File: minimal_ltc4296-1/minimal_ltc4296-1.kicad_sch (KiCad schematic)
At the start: 28 parts, among them Q1 100.0 V, Q2 100.0 V, Q3 100.0 V, U1 LTC4296AUK-1-PBF

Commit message: Update KiCad PCB and schematic files
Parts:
- added Q4, Q5: 100.0 V, transistor_footprints:LFPAK33-8, symbol TRANSISTORS_PSMN075-100MSEX_DATA_BASE:Q_PSMN075-100MSEX
- added Q6: 100.0 V, transistor_footprints:LFPAK33-8, symbol TRANSISTORS_PSMN040-100MSEX_DATA_BASE:Q_PSMN040-100MSEX
- added R17, R18: 24 mΩ, resistor_footprints:R_0612_1632Metric, symbol RESISTORS_ERJ-B2CF_DATA_BASE:R_ERJ-B2CFR024V
- added R19: 390 mΩ, resistor_footprints:R_0612_1632Metric, symbol RESISTORS_ERJ-B2BF_DATA_BASE:R_ERJ-B2BFR39V
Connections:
- net GND: no longer Q1.4 (G), U1.23 (LGATE)
- net PSE: now also U1.4 (HSNSP0), U1.44 (HSNSP2), U1.48 (HSNSP1), R17.1, R18.1, R19.1
- net OUTP0: now reaches U1.1 (OUTP0)
- net OUTP0: now also Q5.1 (S), Q5.2 (S), Q5.3 (S)
- net HGATE0: now reaches U1.2 (HGATE0)
- net HGATE0: now also Q5.4 (G)
- net HSNSM0: now reaches U1.3 (HSNSM0)
- net HSNSM0: now also Q5.5 (D), R18.2
- net OUTP2: now reaches U1.41 (OUTP2)
- net OUTP2: now also Q4.1 (S), Q4.2 (S), Q4.3 (S)
- net HGATE2: now reaches U1.42 (HGATE2)
- net HGATE2: now also Q4.4 (G)
- net HSNSM2: now reaches U1.43 (HSNSM2)
- net HSNSM2: now also Q4.5 (D), R17.2
- net OUTP1: now reaches U1.45 (OUTP1)
- net OUTP1: now also Q6.1 (S), Q6.2 (S), Q6.3 (S)
- net HGATE1: now reaches U1.46 (HGATE1)
- net HGATE1: now also Q6.4 (G)
- net HSNSM1: now reaches U1.47 (HSNSM1)
- net HSNSM1: now also Q6.5 (D), R19.2
- new net: Q1.4 (G), U1.23 (LGATE)

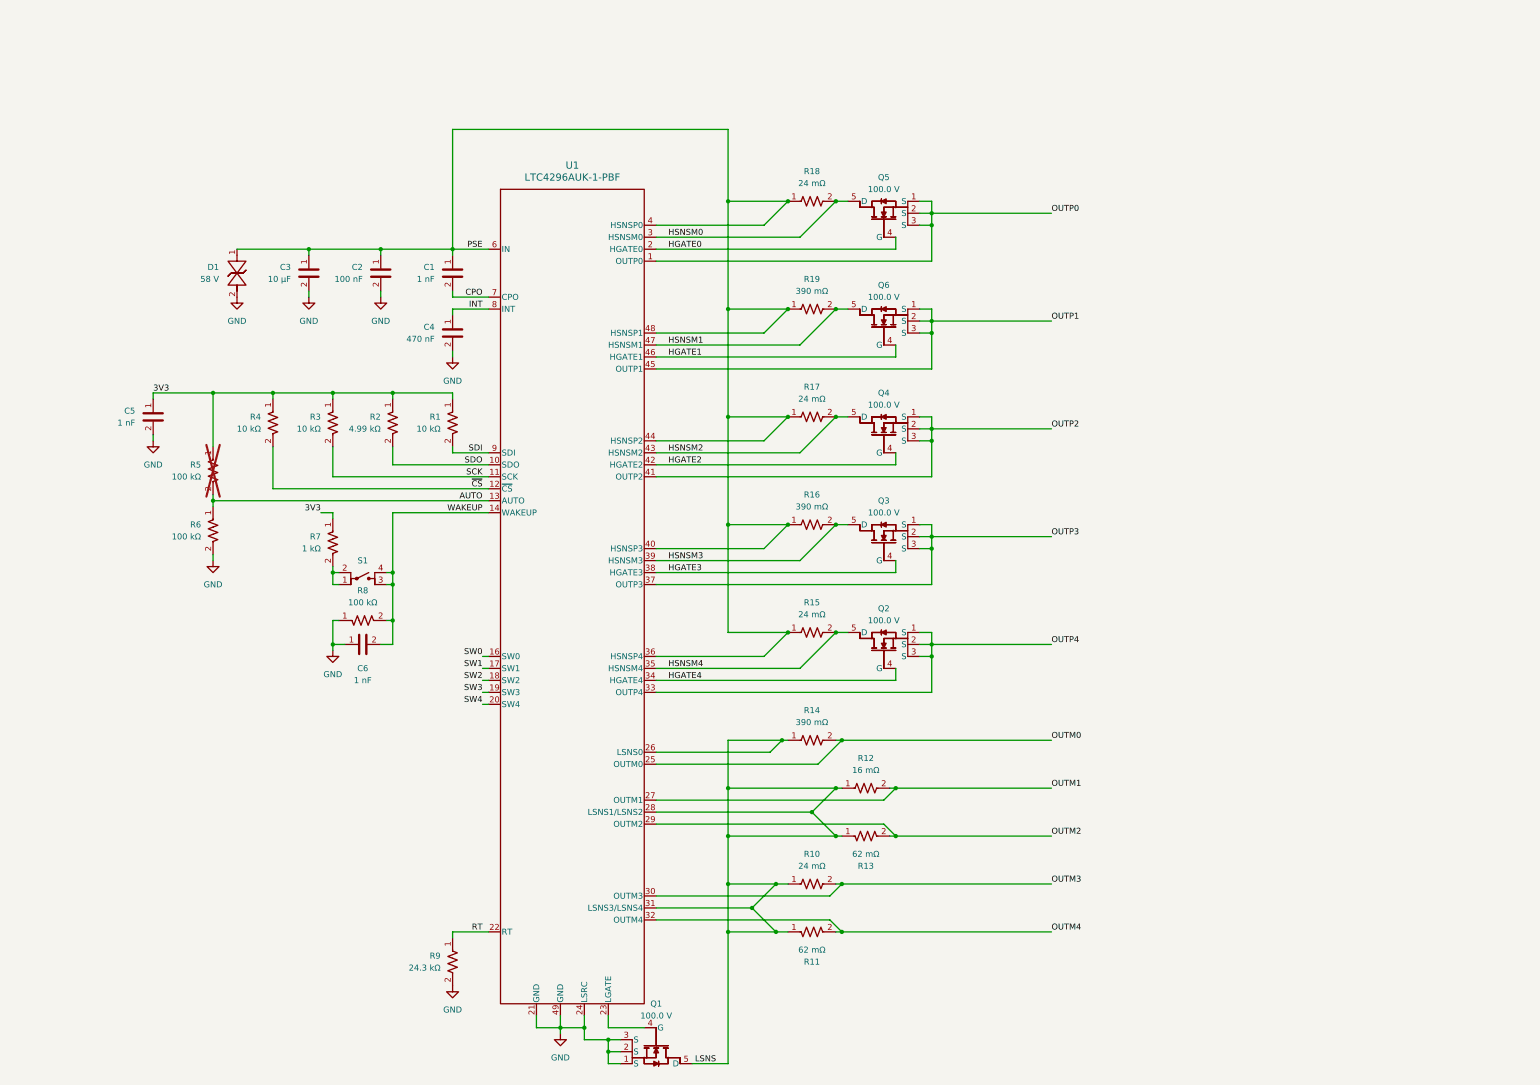
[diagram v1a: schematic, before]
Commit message: Update KiCAD files and generator
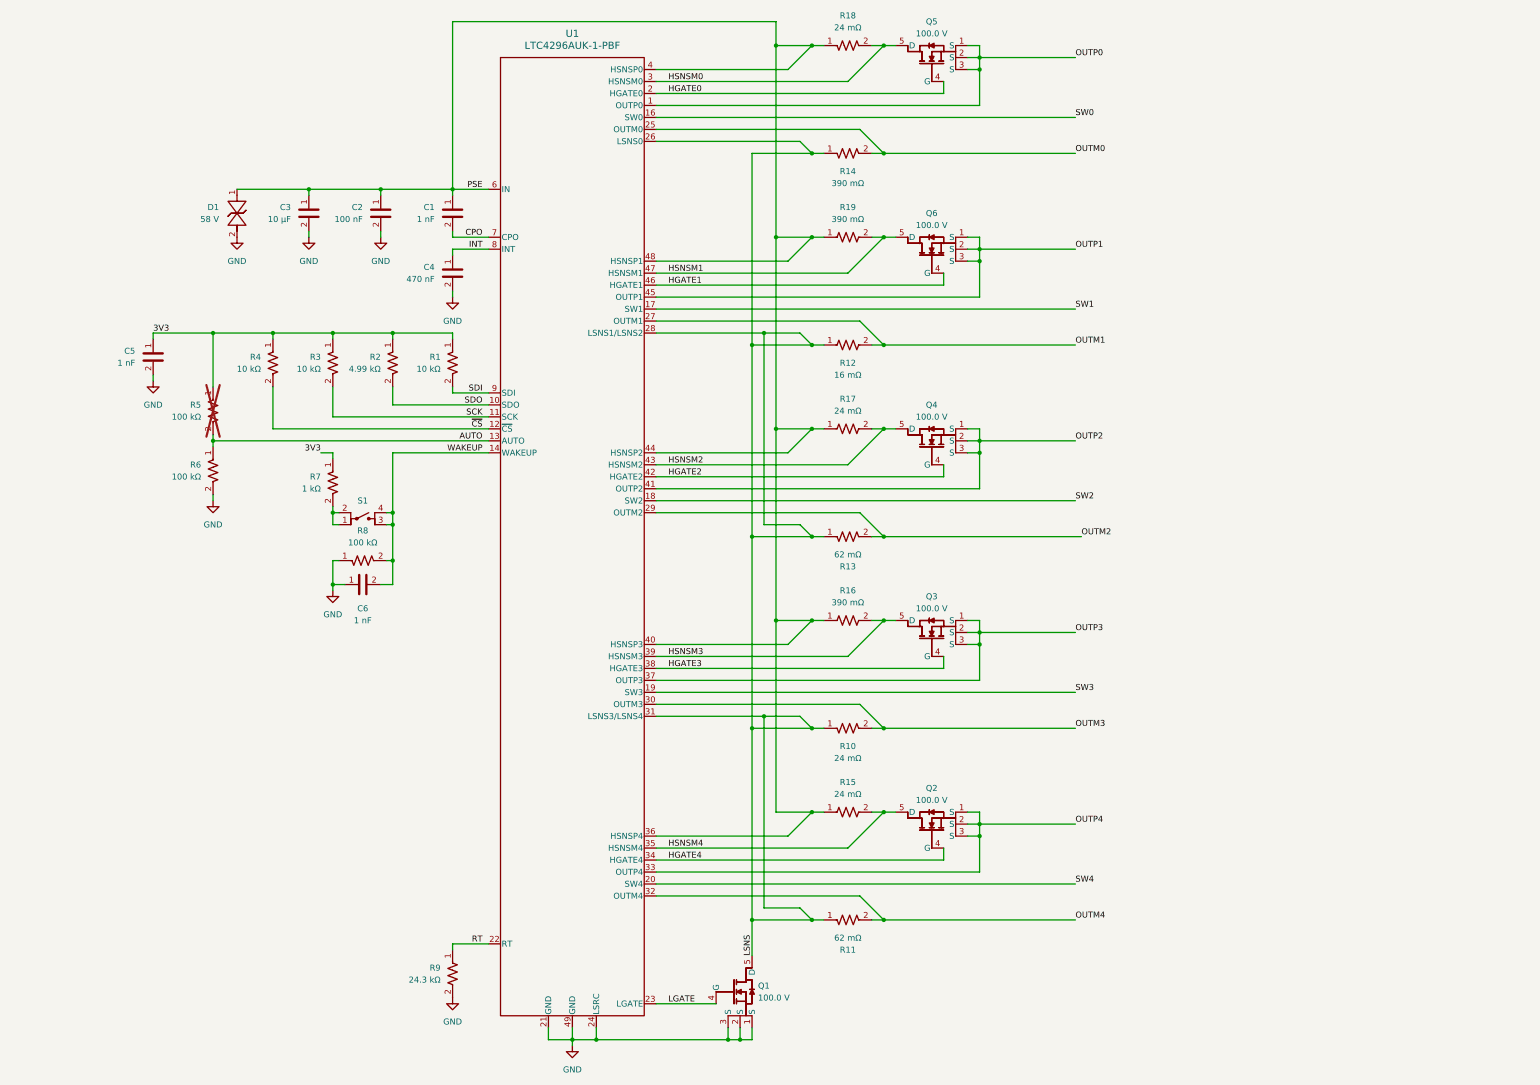
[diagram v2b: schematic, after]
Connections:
- net LGATE: now reaches Q1.4 (G), U1.23 (LGATE)
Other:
- moved on the sheet: C1, C2, C3, C4, C5, C6, D1, Q1, Q2, Q3, Q4, Q5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

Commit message: Update PCB layout and schematic, refresh symbol library
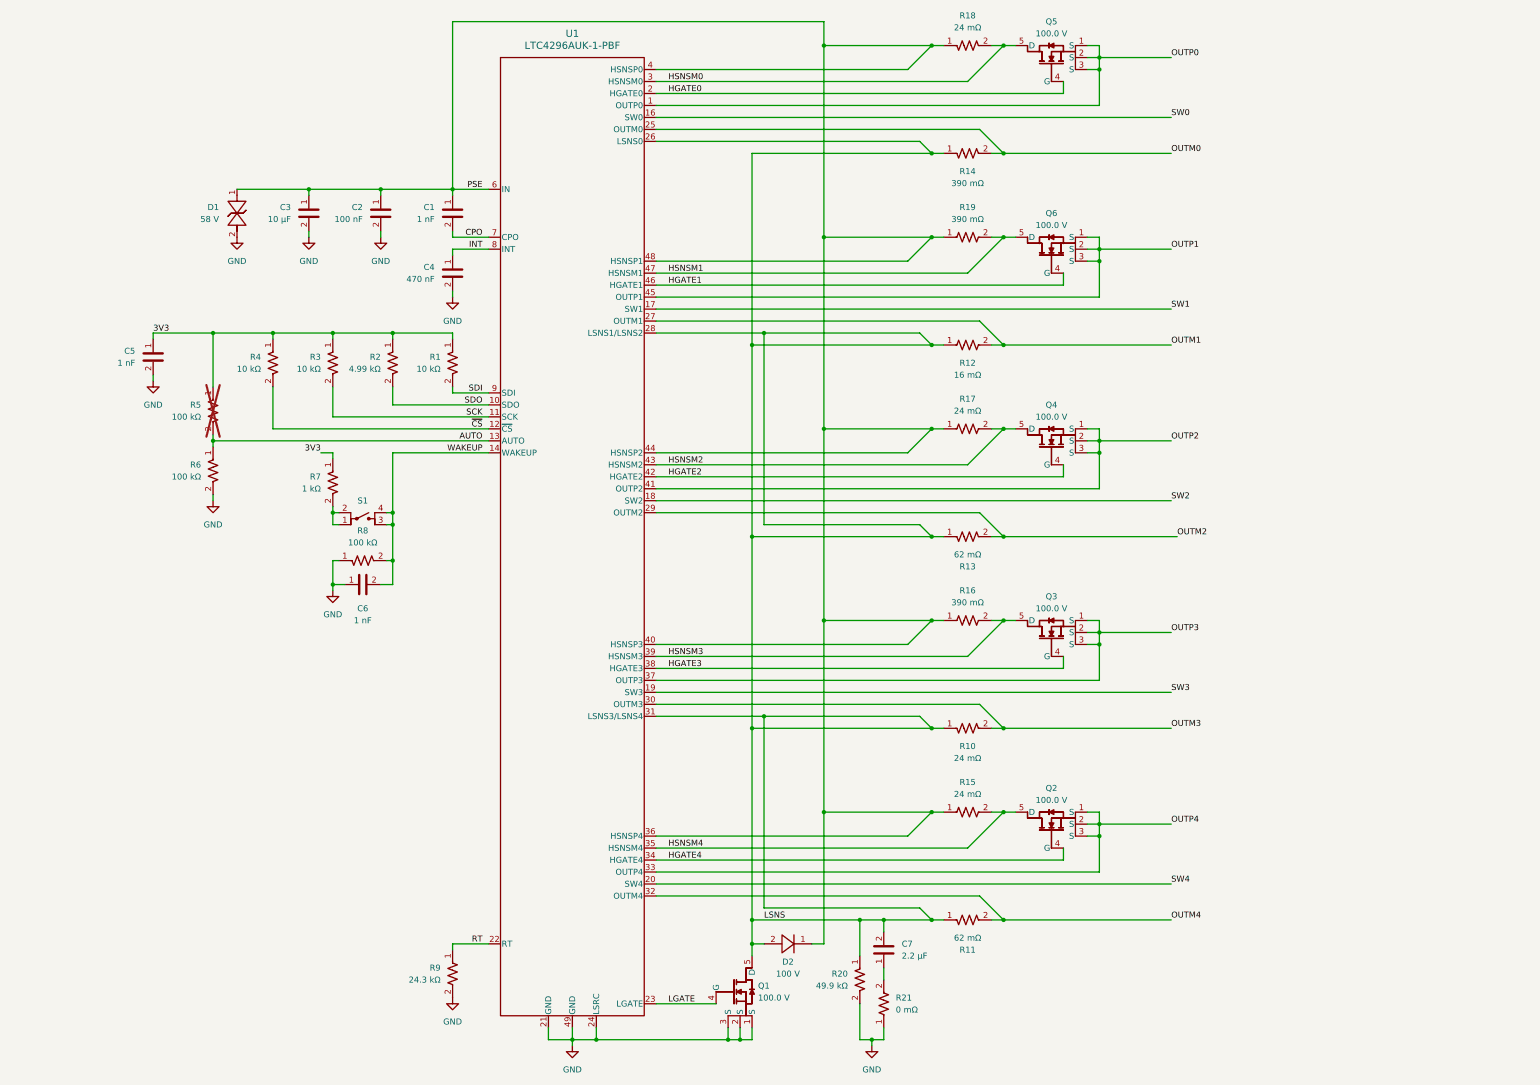
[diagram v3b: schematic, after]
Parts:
- added C7: 2.2 µF, capacitor_footprints:C_1206_3216Metric, symbol CAPACITORS_CL31B_DATA_BASE:C_CL31B225KBHNNN#
- added D2: 100 V, diode_footprints:SMA, symbol DIODES_S1B-13-F_DATA_BASE:D_S1B-13-F
- added R20: 49.9 kΩ, resistor_footprints:R_0402_1005Metric, symbol RESISTORS_ERJ-2RKF_DATA_BASE:R_ERJ-2RKF4992X
- added R21: 0 mΩ, resistor_footprints:R_0603_1608Metric, symbol RESISTORS_ERJ-3GEY0_DATA_BASE:R_ERJ-3GEY0R00V
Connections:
- net GND: now also R20.2, R21.1
- net LSNS: now also C7.2, D2.2, R20.1
- net PSE: now also D2.1
- new net: C7.1, R21.2
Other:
- moved on the sheet: Q2, Q3, Q4, Q5, Q6, R10, R11, R12, R13, R14, R15, R16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

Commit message: Update PCB layout and schematic
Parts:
- added J1, J2, J3, J4, J5: TBP02R1-381-03BE, connector_footprints:TBP02R1-381-03BE, symbol CONNECTORS_TBP02R1-381_DATA_BASE:J_TBP02R1-381-03BE
- C7: footprint capacitor_footprints:C_1206_3216Metric -> capacitor_footprints:C_0805_2012Metric; symbol CAPACITORS_CL31B_DATA_BASE:C_CL31B225KBHNNN# -> CAPACITORS_CGA4J1X7R2A_DATA_BASE:C_CGA4J1X7R2A225K125AC; Case Code - in 1206 -> 0805; Case Code - mm 3216 -> 2012; MPN CL31B225KBHNNN# -> CGA4J1X7R2A225K125AC; Manufacturer Samsung Electro-Mechanics -> TDK; Series CL31B -> CGA4J1X7R2A; Symbol Name C_CL31B225KBHNNN# -> C_CGA4J1X7R2A225K125AC; Trustedparts Search https://www.trustedparts.com/en/search/CL31/CL31B225KBHNNN# -> https://www.trustedparts.com/en/search/CGA4J1X7R2A225K125AC; Voltage Rating 50V -> 100V
- R20: footprint resistor_footprints:R_0402_1005Metric -> resistor_footprints:R_0805_2012Metric; symbol RESISTORS_ERJ-2RKF_DATA_BASE:R_ERJ-2RKF4992X -> RESISTORS_ERJ-6ENF_DATA_BASE:R_ERJ-6ENF4992V; Case Code - in 0402 -> 0805; Case Code - mm 1005 -> 2012; MPN ERJ-2RKF4992X -> ERJ-6ENF4992V; Series ERJ-2RKF -> ERJ-6ENF; Symbol Name R_ERJ-2RKF4992X -> R_ERJ-6ENF4992V; Trustedparts Search https://www.trustedparts.com/en/search/ERJ-2RKF4992X -> https://www.trustedparts.com/en/search/ERJ-6ENF4992V; Voltage Rating 50V -> 150V
- R21: footprint resistor_footprints:R_0603_1608Metric -> resistor_footprints:R_0805_2012Metric; symbol RESISTORS_ERJ-3GEY0_DATA_BASE:R_ERJ-3GEY0R00V -> RESISTORS_ERJ-6GEY0_DATA_BASE:R_ERJ-6GEY0R00V; Case Code - in 0603 -> 0805; Case Code - mm 1608 -> 2012; MPN ERJ-3GEY0R00V -> ERJ-6GEY0R00V; Series ERJ-3GEY0 -> ERJ-6GEY0; Symbol Name R_ERJ-3GEY0R00V -> R_ERJ-6GEY0R00V; Trustedparts Search https://www.trustedparts.com/en/search/ERJ-3GEY0R00V -> https://www.trustedparts.com/en/search/ERJ-6GEY0R00V; Voltage Rating 75V -> 150V
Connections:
- net OUTM0: now also J1.2
- net OUTM1: now also J4.2
- net OUTM2: now also J3.2
- net OUTM3: now also J5.2
- net OUTM4: now also J2.2
- net OUTP0: now also J1.1
- net OUTP1: now also J4.1
- net OUTP2: now also J3.1
- net OUTP3: now also J5.1
- net OUTP4: now also J2.1

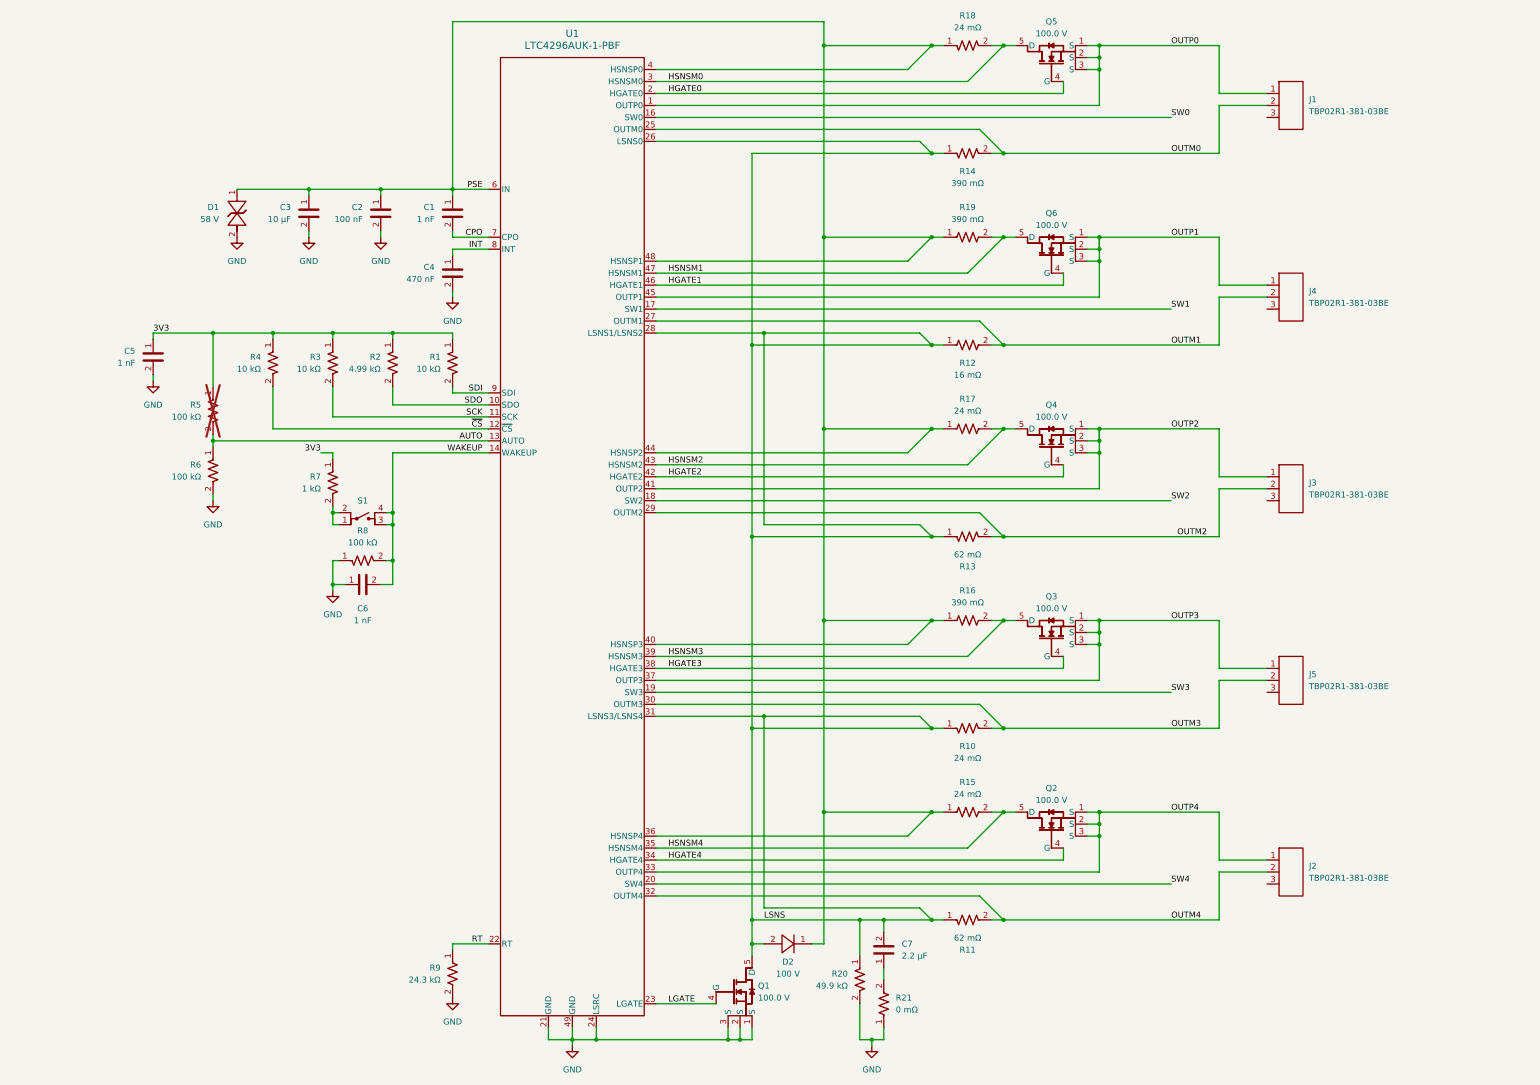
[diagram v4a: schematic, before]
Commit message: Update PCB and schematic files, and KiCAD symbols generator
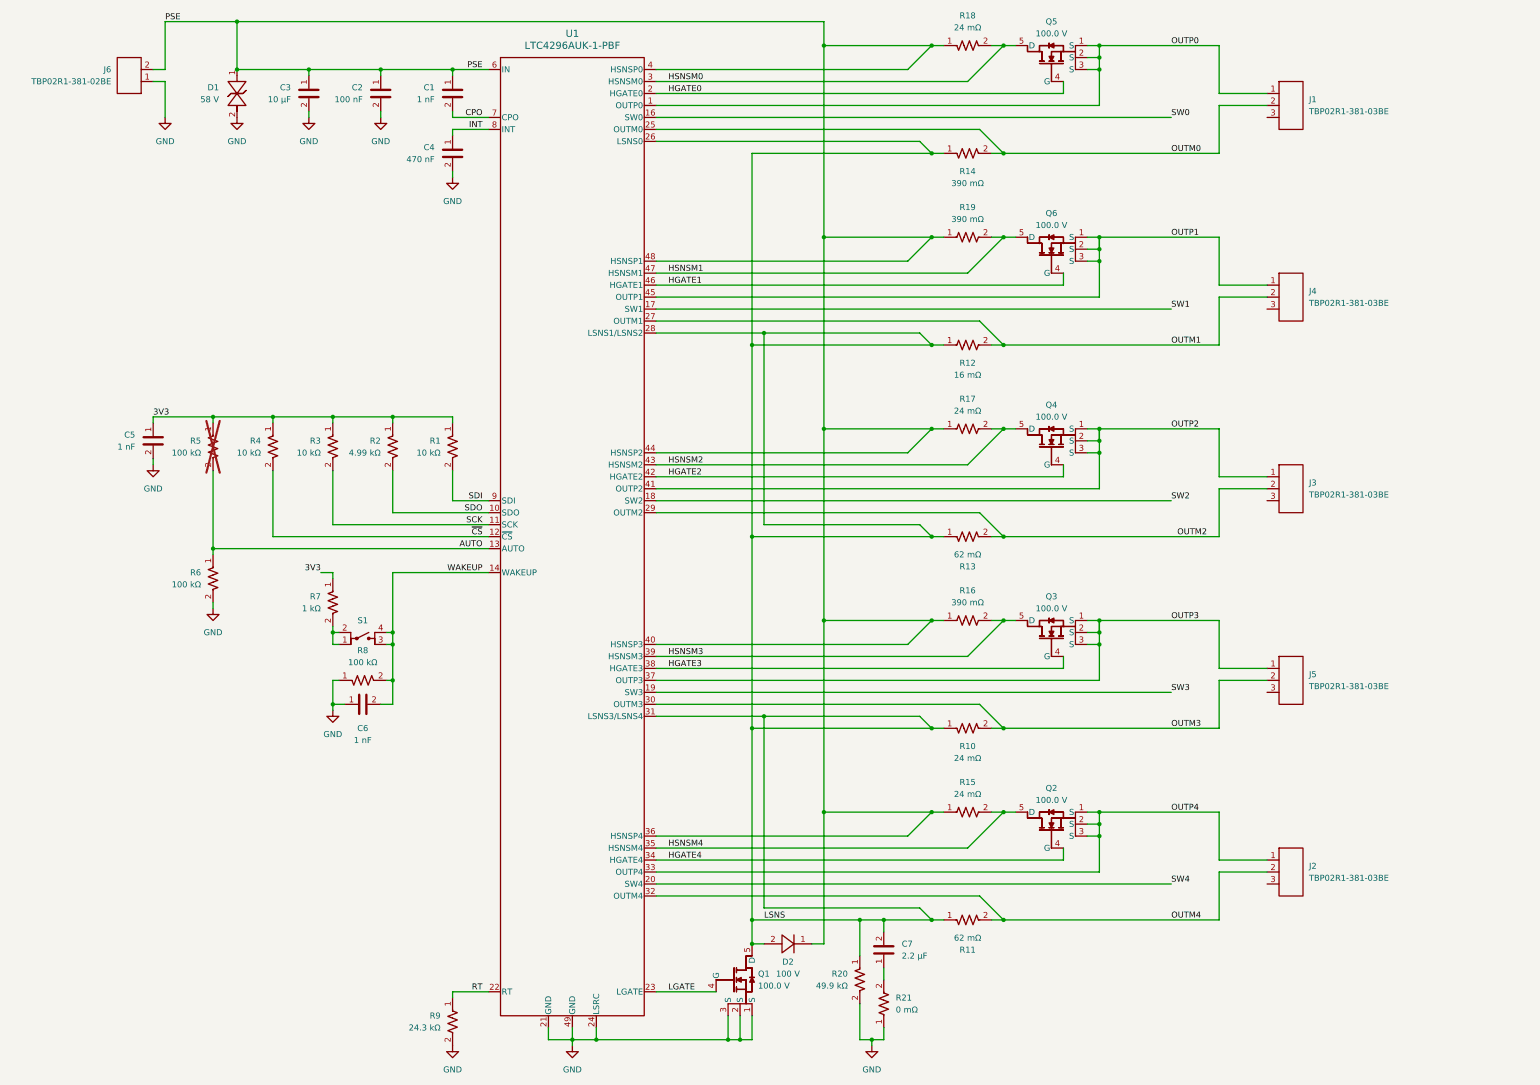
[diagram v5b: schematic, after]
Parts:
- added J6: TBP02R1-381-02BE, connector_footprints:TBP02R1-381-02BE, symbol CONNECTORS_TBP02R1-381_DATA_BASE:J_TBP02R1-381-02BE
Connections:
- net GND: now also J6.1
- net PSE: now also J6.2
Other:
- moved on the sheet: C1, C2, C3, C4, C5, C6, D1, Q1, R1, R2, R3, R4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
